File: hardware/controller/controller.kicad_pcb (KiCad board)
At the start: 2 copper layers, 125 x 95 mm, 63 parts, among them J1 USB_C_Receptacle_USB2.0_16P, J2 Micro_SD_Card_Det_Hirose_DM3AT, J3 Display, J4 Tranceiver Data, J5 Tranceiver Boot/Rst, Q1 AO3400A, SW1 Reset, SW2 Boot, SW3 SW_SPDT, SW4 BTN_1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

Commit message: changed switch circuit
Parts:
- moved Q1 9.50 mm to (127.3, 133.2), turned to -90 degrees
- moved C13 4.72 mm to (118.2, 151.9)
- moved C26 3.30 mm to (161.8, 128.8), turned to 90 degrees
- moved C17 2.75 mm to (122.9, 127.7)
- moved C18 2.75 mm to (124.3, 131.5)
- moved U3 2.75 mm to (128.2, 126.9)
- moved C23 1.90 mm to (161.8, 131.4), turned to 90 degrees
- moved SW4 1.32 mm to (160.0, 128.8)
- moved SW5 0.11 mm to (160.0, 131.4)
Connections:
- C18 pad 1: VCC -> Net-(Q1-S)
- Q1 pad 2: GND -> Net-(Q1-S)
- Q1 pad 3: Net-(Q1-D) -> VCC
- U3 pad 1: Net-(Q1-D) -> GND
- U3 pad 3: VCC -> Net-(Q1-S)
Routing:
- net GND: track 50.8 -> 54.8 mm, vias 179 -> 184
- net Net-(Q1-S): track 0.00 -> 3.92 mm
- net Net-(Q1-D): track 3.22 -> 0.00 mm
- net +3.3V: track 320.6 -> 323.0 mm
- net Net-(Q1-G): track 17.6 -> 15.2 mm
- net VCC: track 47.7 -> 45.4 mm
- net /BTN_1: track 9.72 -> 7.97 mm

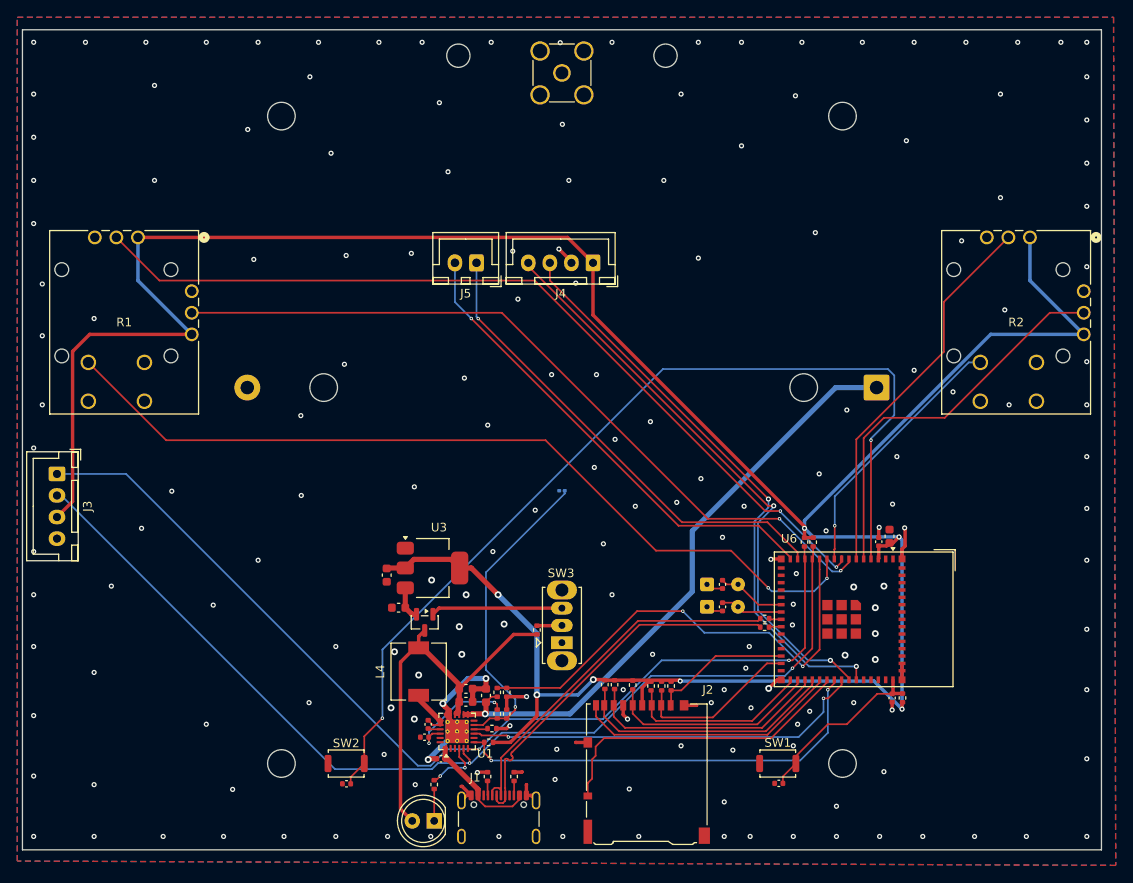
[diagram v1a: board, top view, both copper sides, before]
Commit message: fixed switch and joysticks
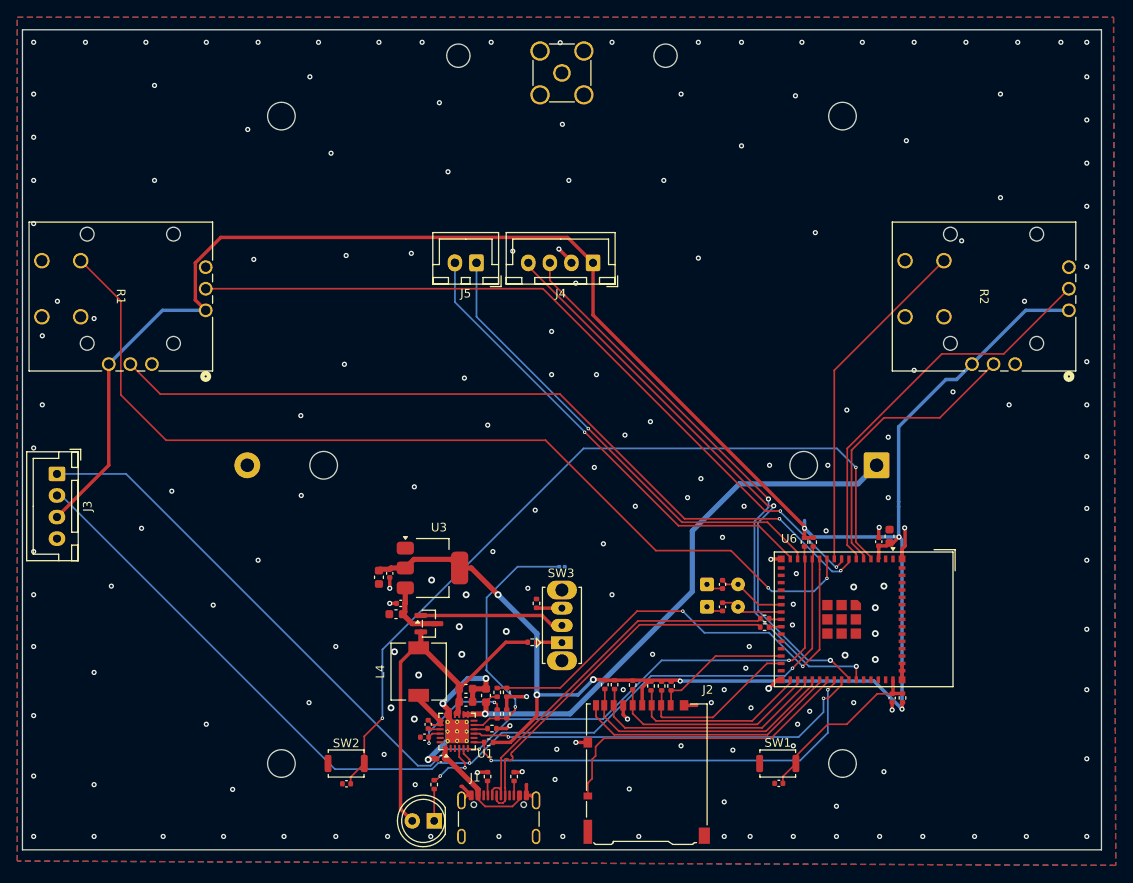
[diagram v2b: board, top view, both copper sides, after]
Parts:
- added C1: 0.1uF, Capacitor_SMD:C_0402_1005Metric, F.Cu at (124.5, 131.0)
- added C2: 0.1uF, Capacitor_SMD:C_0402_1005Metric, F.Cu at (123.2, 127.5)
- added R4: 100, Resistor_SMD:R_0402_1005Metric, F.Cu at (140.2, 131.0)
- Q1: value AO3400A -> AO3401A
- R27: value 10K -> 100
- moved R1 11.5 mm to (101.9, 97.0), turned to -90 degrees
- moved R2 9.58 mm to (201.9, 97.0), turned to -90 degrees
- moved BT1 9.00 mm to (179.7, 115.0)
- moved TH1 8.80 mm to (143.2, 126.8), turned to 0 degrees
- moved R27 1.51 mm to (139.8, 135.5), turned to 0 degrees
- moved C17 0.93 mm to (122.0, 128.0)
- moved C18 0.81 mm to (124.0, 132.2)
- moved Q1 0.51 mm to (127.8, 133.3), turned to 0 degrees
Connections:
- C18 pad 1: Net-(Q1-S) -> Net-(Q1-D)
- Q1 pad 2: Net-(Q1-S) -> VCC
- Q1 pad 3: VCC -> Net-(Q1-D)
- R27 pad 2: Net-(SW3-B) -> Net-(SW3-A)
- SW3 pad 1: unconnected-(SW3-A-Pad1) -> Net-(SW3-A)
- SW3 pad 2: Net-(SW3-B) -> Net-(Q1-G)
- SW3 pad 3: Net-(Q1-G) -> Net-(SW3-C)
- U3 pad 3: Net-(Q1-S) -> Net-(Q1-D)
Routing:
- net +3.3V: track 323.0 -> 293.2 mm
- net /BOOT: track 112.7 -> 94.0 mm
- net /JOY_2_Y: track 100.8 -> 88.0 mm
- net /JOY_2_BTN: track 99.6 -> 111.8 mm
- net /JOY_1_X: track 45.5 -> 33.8 mm
- net /JOY_1_BTN: track 30.6 -> 39.8 mm, vias 1 -> 0
- net Net-(Q1-D): track 0.00 -> 7.60 mm
- net Net-(U1-TS): track 36.1 -> 29.9 mm
- net /JOY_2_X: track 89.6 -> 94.2 mm
- net Net-(BT1-+): track 71.1 -> 66.7 mm
- net Net-(Q1-S): track 3.92 -> 0.00 mm
- net Net-(SW3-C): track 0.00 -> 3.03 mm
- net Net-(SW3-A): track 0.00 -> 2.96 mm
- net Net-(SW3-B): track 2.91 -> 0.00 mm
- net GND: track 54.8 -> 56.8 mm, vias 184 -> 190
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
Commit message: fixed usb
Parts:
- R25, R26: value 27K -> 27
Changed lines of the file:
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@@
 			)
 		)
-		(property "Value" "27K"
+		(property "Value" "27"
 			(at 0 1.17 0)
 			(layer "F.Fab")
@@
 			)
 		)
-		(property "Value" "27K"
+		(property "Value" "27"
 			(at 0 1.17 0)
 			(layer "F.Fab")

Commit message: added production files
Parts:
- R19: value 260 -> 200
- TH1: footprint Resistor_SMD:R_0201_0603Metric -> Resistor_SMD:R_0402_1005Metric
- moved TH1 0.25 mm to (143.2, 127.0)
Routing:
- net GND: track 56.8 -> 58.0 mm, vias 190 -> 191
- net +3.3V: track 293.2 -> 292.3 mm

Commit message: added version to silkscreen
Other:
- board text added: "Controller V1.0"
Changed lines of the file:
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@@
 		(layer "Edge.Cuts")
+	)
+	(gr_text "Controller V1.0"
+		(at 82 157.5 0)
+		(layer "F.SilkS")
+		(effects
+			(font
+				(size 1 1)
+				(thickness 0.2)
+				(bold yes)
+			)
+			(justify left bottom)
+		)
 	)
 	(segment

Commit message: rewrote firmware
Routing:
- net GND: track 58.0 -> 62.2 mm, vias 191 -> 190
